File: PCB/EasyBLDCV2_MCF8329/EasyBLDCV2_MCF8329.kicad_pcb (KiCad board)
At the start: 4 copper layers, 72.4 x 45.7 mm, 72 parts, among them J1 10159560-A00221RLF, Q1 CSD17573Q5B, Q2 CSD17573Q5B, Q3 CSD17573Q5B, Q4 CSD17573Q5B, Q5 CSD17573Q5B, Q6 CSD17573Q5B, U1 MCF8329A1IREER

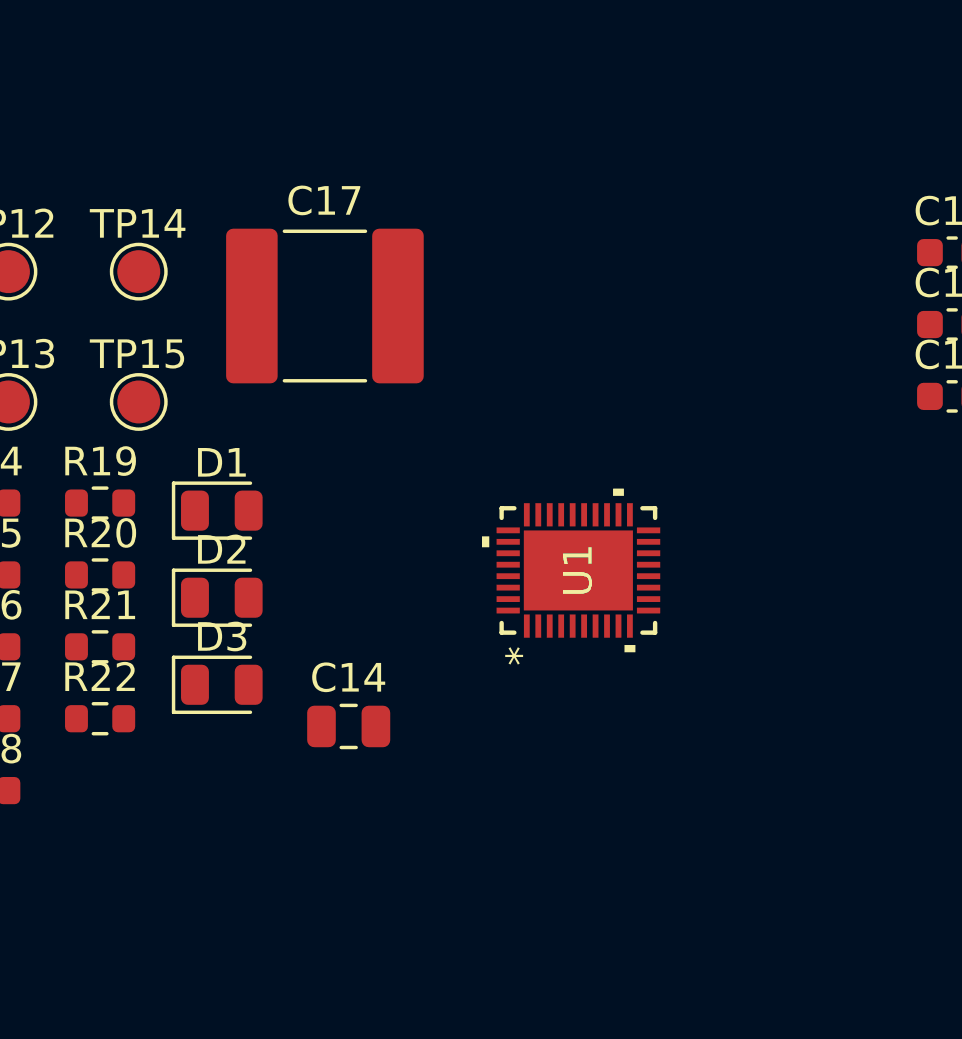
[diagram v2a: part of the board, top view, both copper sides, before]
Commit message: Started component layout
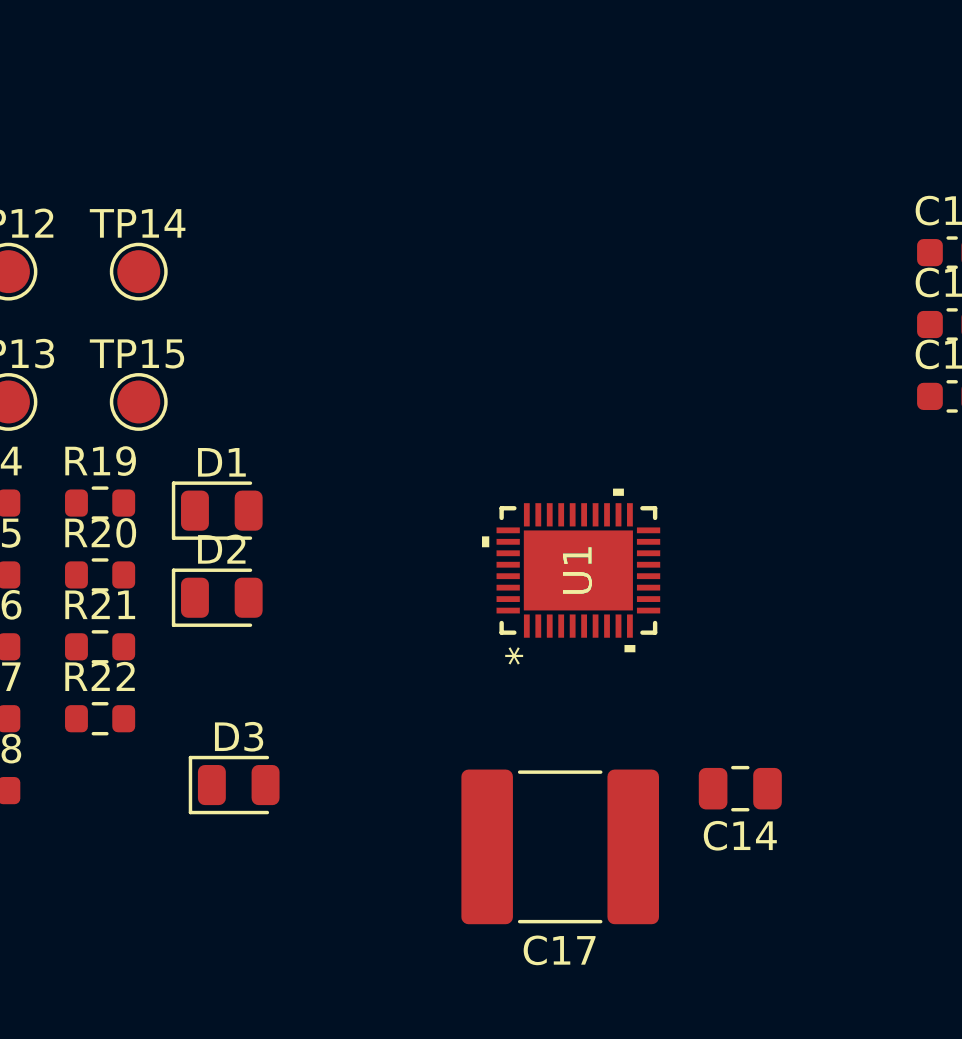
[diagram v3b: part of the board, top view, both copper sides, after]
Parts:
- moved C17 20.6 mm to (64.6, 151.1), turned to 180 degrees
- moved C14 13.8 mm to (70.9, 149.1), turned to 180 degrees
- moved D3 3.55 mm to (53.4, 149.0)
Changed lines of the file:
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@@
 	(footprint "Capacitor_SMD:C_2220_5750Metric"
 		(layer "F.Cu")
-		(at 56.428 132.245)
+		(at 64.643 151.13 180)
 		(descr "Capacitor SMD 2220 (5750 Metric), square (rectangular) end terminal, IPC-7351 nominal, (Body size from: http://datasheets.avx.com/AVX-HV_MLCC.pdf), generated with kicad-footprint-generator")
 		(tags "capacitor")
 		(property "Reference" "C17"
-			(at 0 -3.65 0)
+			(at 0 -3.65 360)
 			(layer "F.SilkS")
 			(effects
@@
 		)
 		(property "Value" "10u"
-			(at 0 3.65 0)
+			(at 0 3.65 360)
 			(layer "F.Fab")
 			(effects
@@
 		)
 		(property "Footprint" "Capacitor_SMD:C_2220_5750Metric"
-			(at 0 0 0)
+			(at 0 0 180)
 			(unlocked yes)
 			(layer "F.Fab")
@@
 		)
 		(property "Datasheet" ""
-			(at 0 0 0)
+			(at 0 0 180)
 			(unlocked yes)
 			(layer "F.Fab")
@@
 		)
 		(property "Description" "Unpolarized capacitor"
-			(at 0 0 0)
+			(at 0 0 180)
 			(unlocked yes)
 			(layer "F.Fab")
@@
 		(attr smd)
 		(fp_line
-			(start -1.415748 -2.61)
-			(end 1.415748 -2.61)
+			(start -1.415748 2.61)
+			(end 1.415748 2.61)
 			(stroke
 				(width 0.12)
@@
 		)
 		(fp_line
-			(start -1.415748 2.61)
-			(end 1.415748 2.61)
+			(start -1.415748 -2.61)
+			(end 1.415748 -2.61)
 			(stroke
 				(width 0.12)
@@
 		)
 		(fp_line
-			(start -3.7 -2.95)
-			(end 3.7 -2.95)
+			(start 3.7 2.95)
+			(end -3.7 2.95)
 			(stroke
 				(width 0.05)
@@
 		)
 		(fp_line
-			(start -3.7 2.95)
-			(end -3.7 -2.95)
+			(start 3.7 -2.95)
+			(end 3.7 2.95)
 			(stroke
 				(width 0.05)
@@
 		)
 		(fp_line
-			(start 3.7 -2.95)
-			(end 3.7 2.95)
+			(start -3.7 2.95)
+			(end -3.7 -2.95)
 			(stroke
 				(width 0.05)
@@
 		)
 		(fp_line
-			(start 3.7 2.95)
-			(end -3.7 2.95)
+			(start -3.7 -2.95)
+			(end 3.7 -2.95)
 			(stroke
 				(width 0.05)
@@
 		)
 		(fp_line
-			(start -2.85 -2.5)
-			(end 2.85 -2.5)
+			(start 2.85 2.5)
+			(end -2.85 2.5)
 			(stroke
 				(width 0.1)
@@
 		)
 		(fp_line
-			(start -2.85 2.5)
-			(end -2.85 -2.5)
+			(start 2.85 -2.5)
+			(end 2.85 2.5)
 			(stroke
 				(width 0.1)
@@
 		)
 		(fp_line
-			(start 2.85 -2.5)
-			(end 2.85 2.5)
+			(start -2.85 2.5)
+			(end -2.85 -2.5)
 			(stroke
 				(width 0.1)
@@
 		)
 		(fp_line
-			(start 2.85 2.5)
-			(end -2.85 2.5)
+			(start -2.85 -2.5)
+			(end 2.85 -2.5)
 			(stroke
 				(width 0.1)
@@
 		)
 		(fp_text user "${REFERENCE}"
-			(at 0 0 0)
+			(at 0 0 360)
 			(layer "F.Fab")
 			(effects
@@
 		)
 		(pad "1" smd roundrect
-			(at -2.55 0)
+			(at -2.55 0 180)
 			(size 1.8 5.4)
 			(layers "F.Cu" "F.Paste" "F.Mask")
@@
 		)
 		(pad "2" smd roundrect
-			(at 2.55 0)
+			(at 2.55 0 180)
 			(size 1.8 5.4)
 			(layers "F.Cu" "F.Paste" "F.Mask")
@@
 	(footprint "Capacitor_SMD:C_0805_2012Metric"
 		(layer "F.Cu")
-		(at 57.258 146.925)
+		(at 70.932 149.098 180)
 		(descr "Capacitor SMD 0805 (2012 Metric), square (rectangular) end terminal, IPC_7351 nominal, (Body size source: IPC-SM-782 page 76, https://www.pcb-3d.com/wordpress/wp-content/uploads/ipc-sm-782a_amendment_1_and_2.pdf, https://docs.google.com/spreadsheets/d/1BsfQQcO9C6DZCsRaXUlFlo91Tg2WpOkGARC1WS5S8t0/edit?usp=sharing), generated with kicad-footprint-generator")
 		(tags "capacitor")
 		(property "Reference" "C14"
-			(at 0 -1.68 0)
+			(at 0 -1.68 360)
 			(layer "F.SilkS")
 			(effects
@@
 		)
 		(property "Value" "470n"
-			(at 0 1.68 0)
+			(at 0 1.68 360)
 			(layer "F.Fab")
 			(effects
@@
 		)
 		(property "Footprint" "Capacitor_SMD:C_0805_2012Metric"
-			(at 0 0 0)
+			(at 0 0 180)
 			(unlocked yes)
 			(layer "F.Fab")
@@
 		)
 		(property "Datasheet" ""
-			(at 0 0 0)
+			(at 0 0 180)
 			(unlocked yes)
 			(layer "F.Fab")
@@
 		)
 		(property "Description" "Unpolarized capacitor"
-			(at 0 0 0)
+			(at 0 0 180)
 			(unlocked yes)
 			(layer "F.Fab")
@@
 		(attr smd)
 		(fp_line
-			(start -0.261252 -0.735)
-			(end 0.261252 -0.735)
+			(start -0.261252 0.735)
+			(end 0.261252 0.735)
 			(stroke
 				(width 0.12)
@@
 		)
 		(fp_line
-			(start -0.261252 0.735)
-			(end 0.261252 0.735)
+			(start -0.261252 -0.735)
+			(end 0.261252 -0.735)
 			(stroke
 				(width 0.12)
@@
 		)
 		(fp_line
-			(start -1.7 -0.98)
-			(end 1.7 -0.98)
+			(start 1.7 0.98)
+			(end -1.7 0.98)
 			(stroke
 				(width 0.05)
@@
 		)
 		(fp_line
-			(start -1.7 0.98)
-			(end -1.7 -0.98)
+			(start 1.7 -0.98)
+			(end 1.7 0.98)
 			(stroke
 				(width 0.05)
@@
 		)
 		(fp_line
-			(start 1.7 -0.98)
-			(end 1.7 0.98)
+			(start -1.7 0.98)
+			(end -1.7 -0.98)
 			(stroke
 				(width 0.05)
@@
 		)
 		(fp_line
-			(start 1.7 0.98)
-			(end -1.7 0.98)
+			(start -1.7 -0.98)
+			(end 1.7 -0.98)
 			(stroke
 				(width 0.05)
@@
 		)
 		(fp_line
-			(start -1 -0.625)
-			(end 1 -0.625)
+			(start 1 0.625)
+			(end -1 0.625)
 			(stroke
 				(width 0.1)
@@
 		)
 		(fp_line
-			(start -1 0.625)
-			(end -1 -0.625)
+			(start 1 -0.625)
+			(end 1 0.625)
 			(stroke
 				(width 0.1)
@@
 		)
 		(fp_line
-			(start 1 -0.625)
-			(end 1 0.625)
+			(start -1 0.625)
+			(end -1 -0.625)
 			(stroke
 				(width 0.1)
@@
 		)
 		(fp_line
-			(start 1 0.625)
-			(end -1 0.625)
+			(start -1 -0.625)
+			(end 1 -0.625)
 			(stroke
 				(width 0.1)
@@
 		)
 		(fp_text user "${REFERENCE}"
-			(at 0 0 0)
+			(at 0 0 360)
 			(layer "F.Fab")
 			(effects
@@
 		)
 		(pad "1" smd roundrect
-			(at -0.95 0)
+			(at -0.95 0 180)
 			(size 1 1.45)
 			(layers "F.Cu" "F.Paste" "F.Mask")
@@
 		)
 		(pad "2" smd roundrect
-			(at 0.95 0)
+			(at 0.95 0 180)
 			(size 1 1.45)
 			(layers "F.Cu" "F.Paste" "F.Mask")
@@
 	(footprint "LED_SMD:LED_0805_2012Metric"
 		(layer "F.Cu")
-		(at 52.828 145.47)
+		(at 53.4185 148.971)
 		(descr "LED SMD 0805 (2012 Metric), square (rectangular) end terminal, IPC_7351 nominal, (Body size source: https://docs.google.com/spreadsheets/d/1BsfQQcO9C6DZCsRaXUlFlo91Tg2WpOkGARC1WS5S8t0/edit?usp=sharing), generated with kicad-footprint-generator")
 		(tags "LED")

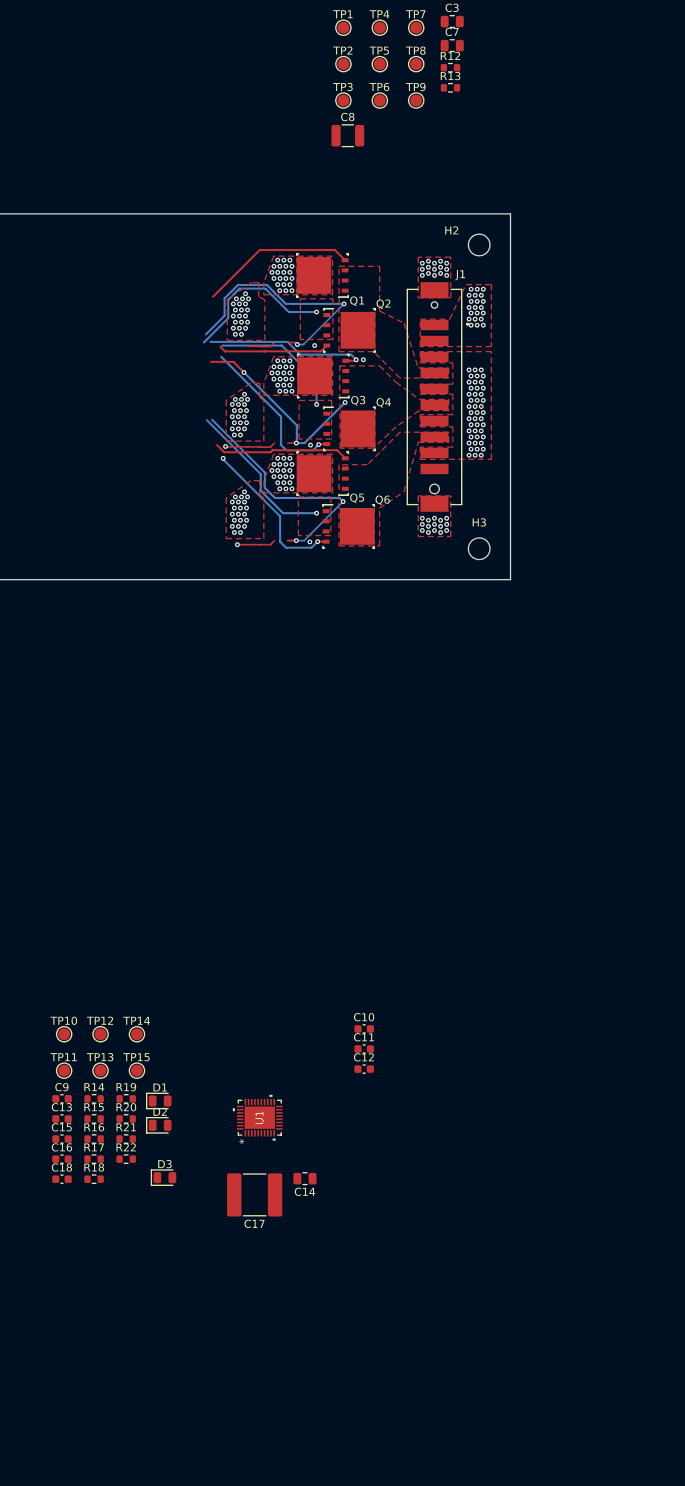
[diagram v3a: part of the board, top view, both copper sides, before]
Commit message: Redid Power Fills
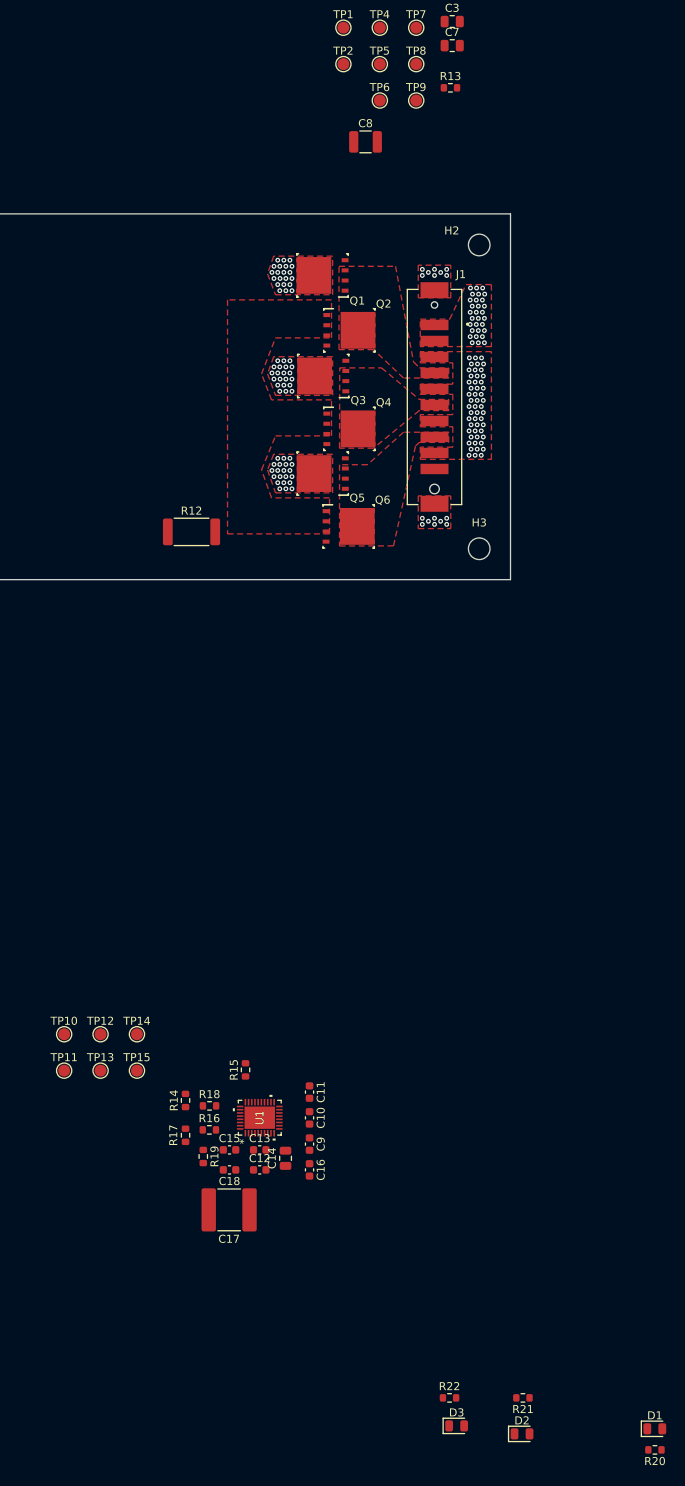
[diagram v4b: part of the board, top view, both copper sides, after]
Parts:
- removed TP3: TestPoint, TestPoint:TestPoint_Pad_D1.5mm
- R12: footprint Resistor_SMD:R_0603_1608Metric -> Resistor_SMD:R_2512_6332Metric
- moved R20 78.0 mm to (114.7, 183.0), turned to 180 degrees
- moved D1 74.2 mm to (114.7, 180.4)
- moved R12 66.4 mm to (56.8, 68.2)
- moved D2 59.4 mm to (98.1, 181.0)
- moved R21 59.2 mm to (98.2, 176.5), turned to 180 degrees
- moved R22 50.2 mm to (89.0, 176.5)
- moved D3 47.9 mm to (89.9, 180.0)
- moved C9 31.5 mm to (71.5, 144.8), turned to -90 degrees
- moved C16 31.0 mm to (71.5, 148.0), turned to -90 degrees
- moved C13 25.0 mm to (65.3, 145.5)
- moved C15 21.0 mm to (61.5, 145.5)
- moved C18 21.0 mm to (61.5, 148.0), turned to 180 degrees
- moved R15 19.9 mm to (63.5, 135.5), turned to 90 degrees
- moved C12 18.1 mm to (65.3, 148.0)
- moved R18 17.1 mm to (59.0, 140.0)
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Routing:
- net MOT_A: track 31.3 -> 0.00 mm, vias 2 -> 0
- net MOT_C: track 30.7 -> 0.00 mm, vias 2 -> 0
- net MOT_B: track 25.5 -> 0.00 mm, vias 3 -> 0
- net Net-(Q3-G): track 20.5 -> 0.00 mm, vias 1 -> 0
- net Net-(Q4-G): track 20.4 -> 0.00 mm, vias 1 -> 0
- net GH_A: track 19.8 -> 0.00 mm, vias 1 -> 0
- net Net-(Q6-G): track 19.6 -> 0.00 mm, vias 2 -> 0
- net Net-(Q1-G): track 19.5 -> 0.00 mm
- net GND: track 19.9 -> 0.44 mm, vias 143 -> 67
- net Net-(Q2-G): track 17.3 -> 0.00 mm
- net Net-(Q5-G): track 16.9 -> 0.00 mm
- net LSS: track 16.6 -> 0.00 mm, vias 1 -> 0
- net (no net): track 6.50 -> 0.07 mm, vias 1 -> 0
- net AVDD: track 4.85 -> 0.00 mm, vias 1 -> 0
- net PVDD: vias 84 -> 93

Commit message: More work on layout
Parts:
- added TP3: TestPoint, TestPoint:TestPoint_Pad_D1.5mm, F.Cu at (57.2, 61.0)
- moved R5 148.6 mm to (82.2, 129.5)
- moved R8 148.6 mm to (82.2, 137.0)
- moved R10 148.6 mm to (82.2, 142.0)
- moved R6 148.6 mm to (82.2, 132.0)
- moved R7 148.6 mm to (82.2, 134.5)
- moved R9 148.6 mm to (82.2, 139.5)
- moved C5 64.2 mm to (68.2, 51.5), turned to -90 degrees
- moved C6 62.1 mm to (68.0, 45.5), turned to 90 degrees
- moved TP9 61.7 mm to (57.2, 69.5)
- moved C7 60.1 mm to (68.2, 63.8), turned to -90 degrees
- moved TP8 55.1 mm to (57.2, 57.5)
- moved C4 51.5 mm to (72.5, 31.5)
- moved TP7 48.7 mm to (57.8, 45.8)
- moved R11 48.6 mm to (56.7, 38.0)
- moved TP6 48.2 mm to (79.0, 62.5)
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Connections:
- U1 pad 11: GHA -> GH_A
- U1 pad 12: GLA -> GL_A
- U1 pad 15: GHB -> GH_B
- U1 pad 16: GLB -> GL_B
- U1 pad 19: GHC -> GH_C
- U1 pad 20: GLC -> GL_C
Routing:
- net AVDD: track 0.00 -> 11.5 mm, vias 0 -> 3
- net GND: track 0.44 -> 10.3 mm, vias 67 -> 97
- net PVDD: track 0.00 -> 9.25 mm, vias 93 -> 61
- net BSTA: track 0.00 -> 6.36 mm
- net MCX_SCL: track 0.00 -> 6.30 mm
- net Net-(U1A-SCL): track 0.00 -> 5.56 mm
- net nFAULT: track 0.00 -> 5.56 mm
- net Net-(U1B-DVDD): track 0.00 -> 5.48 mm
- net Net-(U1A-SHA): track 0.00 -> 5.38 mm
- net Net-(U1B-CPL): track 0.00 -> 5.11 mm
- net Net-(U1B-GVDD): track 0.00 -> 4.89 mm
- net Net-(U1A-SDA): track 0.00 -> 4.88 mm
- net Net-(U1A-SHC): track 0.00 -> 4.84 mm
- net DACOUT/SOX/SPEED_ANA: track 0.00 -> 4.68 mm, vias 0 -> 1
- net BSTC: track 0.00 -> 4.36 mm
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
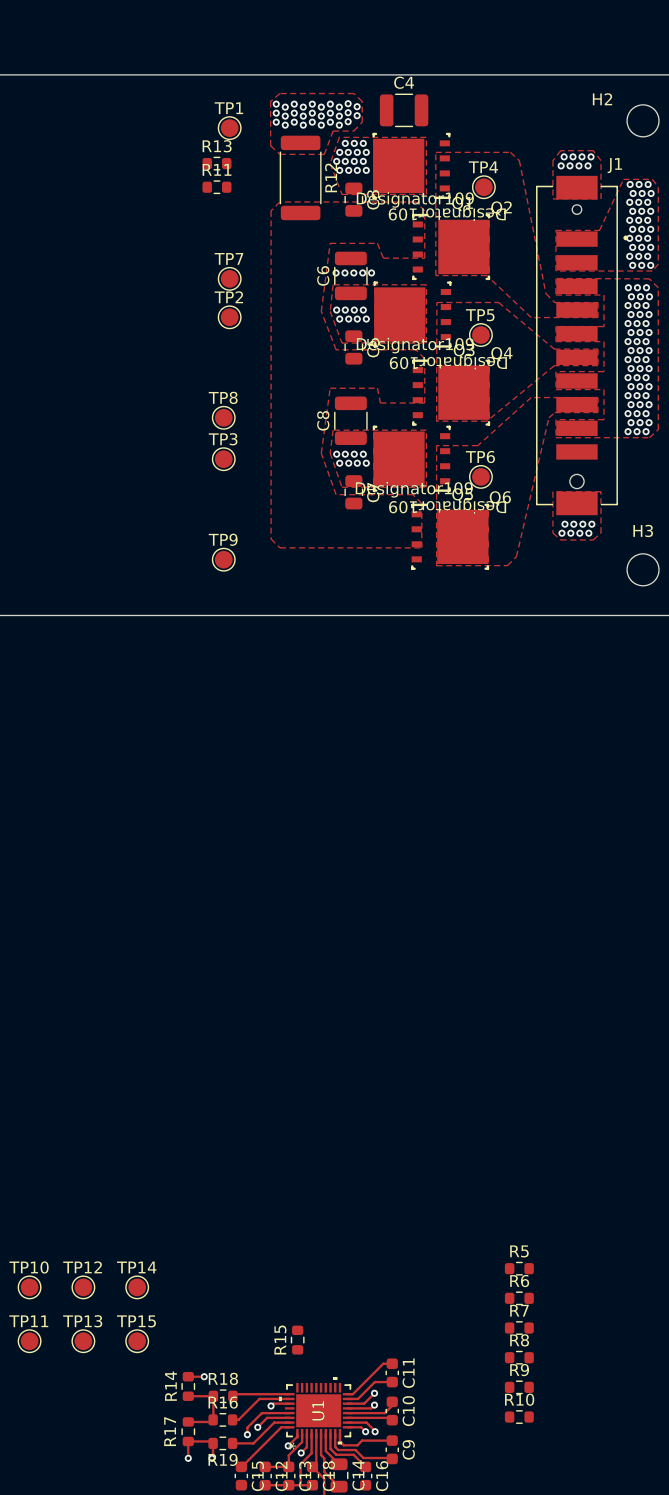
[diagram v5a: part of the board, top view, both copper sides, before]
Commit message: Adjusted power traces
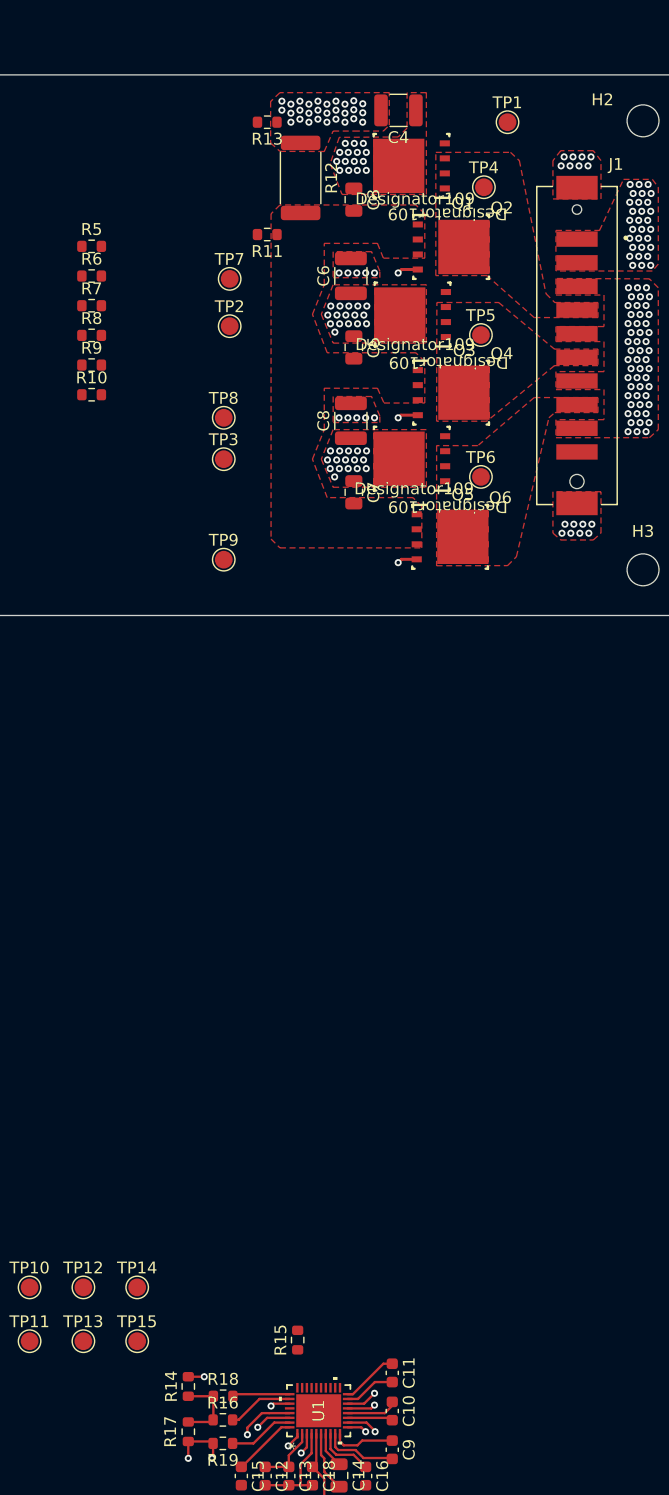
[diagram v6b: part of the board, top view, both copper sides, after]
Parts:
- moved R5 93.7 mm to (46.1, 43.0)
- moved R6 93.7 mm to (46.1, 45.5)
- moved R8 93.7 mm to (46.1, 50.5)
- moved R9 93.7 mm to (46.1, 53.0)
- moved R10 93.7 mm to (46.1, 55.5)
- moved R7 93.7 mm to (46.1, 48.0)
- moved TP1 23.5 mm to (81.2, 32.5)
- moved R11 5.84 mm to (60.9, 42.0), turned to 180 degrees
- moved R13 5.51 mm to (60.9, 32.5), turned to 180 degrees
- moved TP2 0.75 mm to (57.8, 49.8)
- moved C4 0.47 mm to (72.0, 31.5), turned to 180 degrees
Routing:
- net Net-(Q2-G): track 0.00 -> 1.78 mm, vias 0 -> 1
- net Net-(Q4-G): track 0.00 -> 1.75 mm, vias 0 -> 1
- net Net-(Q6-G): track 0.00 -> 1.69 mm, vias 0 -> 1
- net PVDD: vias 61 -> 77
- net GND: vias 97 -> 107
- net (no net): vias 5 -> 0
